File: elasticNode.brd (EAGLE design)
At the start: 58.2 x 52.5 mm, 130 parts, among them J1 FEMALE_HEADER_2X1, J2 JUMPER, J3 ISP_CONN_6PIN, J5 FEMALE_HEADER_10X2, J6 USB_CONNMICRO_SMT, M1 SISS23DN, M2 SISS23DN, M3 SISS23DN, U1 AT90USB128, U10 LTC3419DFN, U11 PAC1720, U14 LTC3419DFN, U2 IS66WV51216EALL, U3 MRF24J40MA, U4 SPARTAN7-LX15, U6 SST26VF032BWDFN, U7 PAC1720, U8 PAC1720, U9 PAC1720, X1 8MHz, X2 50MHz, X3 32MHz, X4 100MHz

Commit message: back up before review.
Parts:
- removed C26: 22u, passive:0805
- removed J3: ISP_CONN_6PIN, connectors:ICSP_SMT
- removed L5: 3.3uH, passive:0805
- removed R29, R30, R44, R45, R48, R49: 1.5k, passive:0805
- removed R37, R38: 1k5, passive:0805
- removed TP4, TP5, TP6: TEST_POINTTHT, connectors:THT
- added C6, C9: 20p, passive:0805
- added D11, D12: GREEN 2.2V, opto:0805
- added J7: USB_CONNMICRO_SMT, connectors:USB_MICRO_B_SMT
- added M4: SISS23DN, power:POWERPAK1212-8
- added MCU_PROGRAM, MON_PROGRAM: ISP_CONN_6PIN, connectors:ICSP_SMT
- added R50, R51: 550, passive:0805
- added R52, R53: 22, passive:0805
- added R54: 15k, passive:0805
- added TP7, TP8: TEST_POINTTHT, connectors:THT
- added U5: ATMEGA32U4QFN, ic:QFN44
- added X5: 8MHz, passive:3.2X2.5_OSC
- moved C30 195.2 mm to (42.4, 27.8)
- moved C34 195.2 mm to (43.1, 24.3)
- moved C38 195.2 mm to (42.4, 18.8)
- moved C39 195.2 mm to (45.2, 18.8)
- moved C32 195.2 mm to (42.4, 13.6)
- moved C35 195.2 mm to (46.6, 25.2)
- moved C36 195.2 mm to (42.4, 21.4)
- moved C37 195.2 mm to (45.2, 21.4)
- moved C40 195.2 mm to (42.4, 16.2)
- moved U2 173.2 mm to (8.30, 29.8)
- moved C20 148.3 mm to (36.2, 36.8)
- moved C24 148.3 mm to (36.9, 25.4)
- moved C25 148.3 mm to (40.4, 26.3)
- moved C29 148.3 mm to (36.2, 22.5)
- moved C31 148.3 mm to (36.2, 19.9)
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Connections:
- net A10 renamed XMEM_A10
- net A11 renamed XMEM_A11
- net A12 renamed XMEM_A12
- net A13 renamed XMEM_A13
- net A14 renamed XMEM_A14
- net A15 renamed XMEM_A15
- net A8 renamed XMEM_A8
- net A9 renamed XMEM_A9
- net RD renamed XMEM_RD
- net WR renamed XMEM_WR
- removed net 1V2: C26.2, L5.2, R37.2, TP3.3
- removed net 1V5: TP6.3
- removed net ENABLE_LEDS: U1.17
- removed net FPGA_RESES: U1.59
- removed net FPGA_SUSPEND: U1.19
- removed net N$21: U4.P4
- removed net N$22: U4.P3
- removed net N$26: U4.L3
- removed net N$31: U4.L2
- removed net N$33: U4.M5
- removed net N$34: U4.M4
- removed net N$35: U4.P5
- removed net N$36: U4.N4
- removed net N$39: U4.H12
- removed net N$40: U4.L5
- removed net N$54: R37.1, R38.2, U14.8
- removed net N$56: L5.1, U14.6
- removed net SRAM_VCC: R23.2, R43.2, U11.2, U4.G2, U4.K2, U4.N2, U7.2, X4.1, X4.4
- new net DAUGHTER_VCC: OUT2.10, R43.2, U11.2
- new net GND1: D11.2, D12.2
- new net MON_LED0: R50.1, U5.20
- new net MON_LED1: R51.1, U5.21
- new net MON_MISO: MON_PROGRAM.1, U5.11
- new net MON_MOSI: MON_PROGRAM.4, U5.10
- new net MON_RESET: MON_PROGRAM.5, R54.2, U5.13
- new net MON_SCK: MON_PROGRAM.3, U5.9
- new net MON_USB_D+: R53.1, U5.4
- new net MON_USB_D-: R52.1, U5.3
- new net MON_USB_VCC: J7.1, U5.7
- new net N$16: D12.1, R51.2
- new net N$17: D11.1, R50.2
- new net N$18: C9.1, U5.17, X5.3
- new net N$19: J7.2, R52.2
- new net N$20: C6.1, U5.16, X5.1
- new net SRAM_POWER: M4.4, U1.2
- new net SRAM_VDD_MON: M4.1, M4.2, M4.3, R23.2, U7.2
- net 1V: now also TP8.3; no longer TP4.3
- net 1V8: now also TP7.3; no longer R43.1, TP2.3, U11.1
- net 3V3: now also MCU_PROGRAM.2, MON_PROGRAM.2, R43.1, R54.1, TP2.3, U11.1, U5.14, U5.2, U5.24, U5.34, U5.44, U5.6; no longer J3.2, OUT2.10, R29.2, R30.2, R44.2, R45.2, R48.2, R49.2, U14.7
- net AD6/SELECTMAP_D1/SPI_MISO/MCU_PDO: now also MCU_PROGRAM.1; no longer J3.1
- net AD7/SELECTMAP_D0/SPI_MOSI/PDI: now also MCU_PROGRAM.4; no longer J3.4
- net FPGA_RESET: now also U1.59
- net GND: now also C2.2, C3.2, C6.2, C9.2, J7.5, MCU_PROGRAM.6, MON_PROGRAM.6, TP3.3, U5.15, U5.23, U5.35, U5.43, U5.45, U5.5; no longer C26.1, J3.6, R38.1, TP5.3
- net MCU_RESET: now also MCU_PROGRAM.5; no longer J3.5
- net MONITORING: now also U5.1
- net N$5: now also J7.3, R53.2; no longer C2.2, C3.2
- net SCL: now also U5.18; no longer R29.1, R44.1, R48.1
- net SDA: now also U5.19; no longer R30.1, R45.1, R49.1
- net SPI_SCK/CCLK: now also MCU_PROGRAM.3; no longer J3.3
- net SRAM_VDD: now also M4.5, M4.6, M4.7, M4.8, U4.G2, U4.K2, U4.N2, X4.1, X4.4

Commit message: Layout work start.
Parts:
- removed C18: 10u, passive:0805
- removed D10: RED, opto:0805
- removed R39: 6k8, passive:0805
- removed R40: 270, passive:0805
- removed R46: 10k, passive:0805
- added C12, C15: 10u, passive:0805
- added J3: JUMPER, connectors:JUMPER_SMT
- added R29, R30: 15k, passive:0805
- added R37: 1k5, passive:0805
- added R38: 6k8, passive:0805
- R31: value 6k8 -> 10k
- R32: value 1k5 -> 6k8
- moved R1 157.5 mm to (204.6, 66.6)
- moved R2 157.5 mm to (204.6, 64.9)
- moved U7 117.0 mm to (93.3, 80.1), flipped to the top, turned to 0 degrees
- moved R26 111.2 mm to (93.4, 77.0), flipped to the top, turned to 0 degrees
- moved D9 107.1 mm to (-20.8, -56.9), turned to 0 degrees
- moved R20 107.0 mm to (89.9, 78.9), flipped to the top
- moved R23 105.8 mm to (89.9, 81.9), flipped to the top
- moved R33 101.6 mm to (-20.8, -54.8), turned to 0 degrees
- moved U11 98.5 mm to (93.3, 60.4)
- moved R43 98.3 mm to (89.9, 62.2), turned to 90 degrees
- moved U8 97.6 mm to (93.3, 73.4), flipped to the top
- moved R27 97.6 mm to (93.4, 70.3), flipped to the top
- moved R36 97.4 mm to (89.9, 59.2), turned to 90 degrees
- moved R42 97.2 mm to (19.5, 99.4)
- moved R41 95.2 mm to (16.7, 99.4)
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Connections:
- removed net N$1: L1.2, U10.4
- removed net N$57: D10.2, R40.2
- removed net N$8: L2.1, U10.6
- new net MON_HWB: J3.1, R30.2, U5.33
- new net N$21: R29.1, U5.2
- new net N$22: L1.1, U10.4
- new net N$26: L2.2, U10.6
- net 1V: now also C17.1, L1.2, R31.2; no longer C27.1, L6.1, R46.2
- net 1V8: now also L2.1, R23.2, R47.1; no longer L2.2, R23.1, R47.2
- net 3V3: now also C12.1, C27.1, L6.1, R24.2, R29.2, R30.1, R38.2, R43.2; no longer C17.1, L1.1, R24.1, R31.1, R43.1, U5.2
- net 5V: now also C15.1; no longer C18.1, D10.1, D9.1
- net DAUGHTER_VCC: now also R43.1; no longer R43.2
- net GND: now also C12.2, C15.2, J3.2, R37.2; no longer C18.2, R39.2, R40.1
- net MONITORING: now also U1.1
- net N$2: now also R31.1; no longer R31.2
- net N$53: now also R37.1, R38.1; no longer R39.1, R46.1
- net N$7: now also R47.2; no longer R47.1
- net SRAM_VDD_MON: now also R23.1; no longer R23.2
- net USB_VCC_RAW: now also D9.1
- net WIRELESS_VCC: now also R24.1; no longer R24.2

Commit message: backup
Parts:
- R29: value 15k -> 0
- moved R1 163.6 mm to (47.4, 21.0)
- moved R2 163.6 mm to (47.4, 19.3)
- moved R54 119.1 mm to (50.6, 41.8), turned to 0 degrees
- moved D9 100.9 mm to (47.4, 17.4), turned to 180 degrees
- moved R29 100.2 mm to (50.6, 40.3)
- moved R33 98.1 mm to (47.4, 15.7), turned to 180 degrees
- moved R26 90.5 mm to (7.20, 49.4), flipped to the bottom, turned to 180 degrees
- moved U7 87.6 mm to (10.9, 50.3), flipped to the bottom
- moved C12 87.1 mm to (28.4, 39.9), turned to 90 degrees
- moved R23 81.2 mm to (14.7, 51.2), flipped to the bottom, turned to 0 degrees
- moved R20 80.8 mm to (14.7, 49.4), flipped to the bottom, turned to 0 degrees
- moved R28 77.1 mm to (17.6, 49.5), flipped to the bottom, turned to 180 degrees
- moved C32 76.4 mm to (12.1, 31.6), flipped to the bottom
- moved R30 75.8 mm to (36.9, 36.7), turned to 0 degrees
- moved U9 73.8 mm to (21.4, 50.3), flipped to the bottom
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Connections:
- net DAUGHTER_VCC: now also R24.1, U8.2; no longer R43.1, U11.2
- net WIRELESS_VCC: now also R43.1, U11.2; no longer R24.1, U8.2
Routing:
- removed copper zone on layer 16, net 1V
- removed copper zone on layer 16, net 3V3
- removed copper zone on layer 16, net 5V
- removed copper zone on layer 16, net N$1
- removed copper zone on layer 16, net N$8
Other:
- board text added: "FPGA LEDS"
- board text added: "MON LEDS"
- board text removed: "FPGA"
- board text removed: "LEDS"

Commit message: backup
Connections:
- net SRAM_A0: no longer U4.D3
- net SRAM_A1: no longer U4.C3
- net SRAM_A10: now also U4.M5; no longer U4.C5
- net SRAM_A11: now also U4.N1; no longer U4.C4
- net SRAM_A12: no longer U4.E4
- net SRAM_A13: no longer U4.D4
- net SRAM_A14: no longer U4.F3
- net SRAM_A15: no longer U4.F2
- net SRAM_A16: no longer U4.G1
- net SRAM_A17: now also U4.N4; no longer U4.F1
- net SRAM_A18: now also U4.M2; no longer U4.E2
- net SRAM_A2: no longer U4.A4
- net SRAM_A3: no longer U4.A3
- net SRAM_A4: now also U4.A5; no longer U4.B3
- net SRAM_A5: now also U4.A4; no longer U4.A2
- net SRAM_A6: now also U4.A3; no longer U4.B5
- net SRAM_A7: now also U4.A2; no longer U4.A5
- net SRAM_A8: now also U4.M3; no longer U4.B2
- net SRAM_A9: now also U4.M4; no longer U4.B1
- net SRAM_CS: no longer U4.B6
- net SRAM_D0: no longer U4.D2
- net SRAM_D1: no longer U4.D1
- net SRAM_D10: now also U4.L1; no longer U4.K3
- net SRAM_D11: now also U4.L2; no longer U4.J4
- net SRAM_D12: now also U4.J1; no longer U4.J3
- net SRAM_D13: now also U4.H1; no longer U4.M1
- net SRAM_D14: now also U4.G1; no longer U4.L1
- net SRAM_D15: now also U4.F1; no longer U4.M3
- net SRAM_D2: no longer U4.C1
- net SRAM_D3: no longer U4.H4
- net SRAM_D4: no longer U4.H3
- net SRAM_D5: no longer U4.H2
- net SRAM_D6: no longer U4.H1
- net SRAM_D7: no longer U4.J2
- net SRAM_D8: now also U4.M1; no longer U4.J1
- net SRAM_D9: now also U4.L3; no longer U4.K4
- net SRAM_LB: now also U4.D1; no longer U4.N1
- net SRAM_OE: now also U4.B1; no longer U4.M2
- net SRAM_UB: now also U4.C1; no longer U4.P2
- net SRAM_WE: no longer U4.F4
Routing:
- net SRAM_VDD: track 0.00 -> 56.4 mm, vias 0 -> 6
- net SRAM_A4: track 0.00 -> 19.8 mm, vias 0 -> 2
- net SRAM_A10: track 0.00 -> 8.77 mm, vias 0 -> 2
- net SRAM_A17: track 0.00 -> 8.73 mm, vias 0 -> 2
- net SRAM_A5: track 0.00 -> 7.04 mm
- net SRAM_A9: track 0.00 -> 6.95 mm, vias 0 -> 2
- net SRAM_D9: track 0.00 -> 6.24 mm, vias 0 -> 2
- net SRAM_A6: track 0.00 -> 6.04 mm
- net SRAM_A8: track 0.00 -> 5.62 mm, vias 0 -> 2
- net SRAM_A7: track 0.00 -> 5.08 mm
- net SRAM_D12: track 0.00 -> 5.06 mm
- net SRAM_A11: track 0.00 -> 4.79 mm
- net SRAM_D11: track 0.00 -> 4.77 mm, vias 0 -> 2
- net SRAM_A18: track 0.00 -> 4.46 mm, vias 0 -> 2
- net SRAM_D10: track 0.00 -> 4.04 mm
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
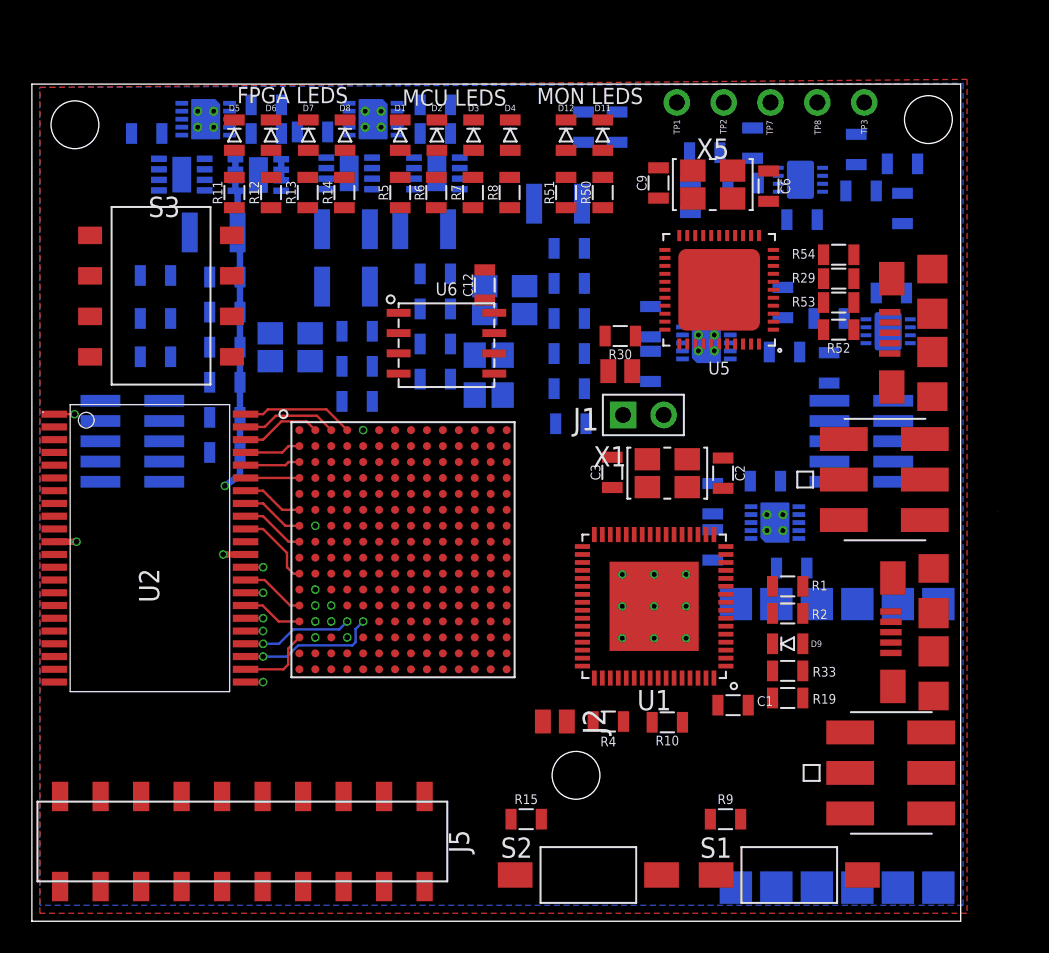
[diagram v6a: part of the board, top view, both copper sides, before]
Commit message: backup
SRAM and FPGA finished, now connecting fpga and MCU
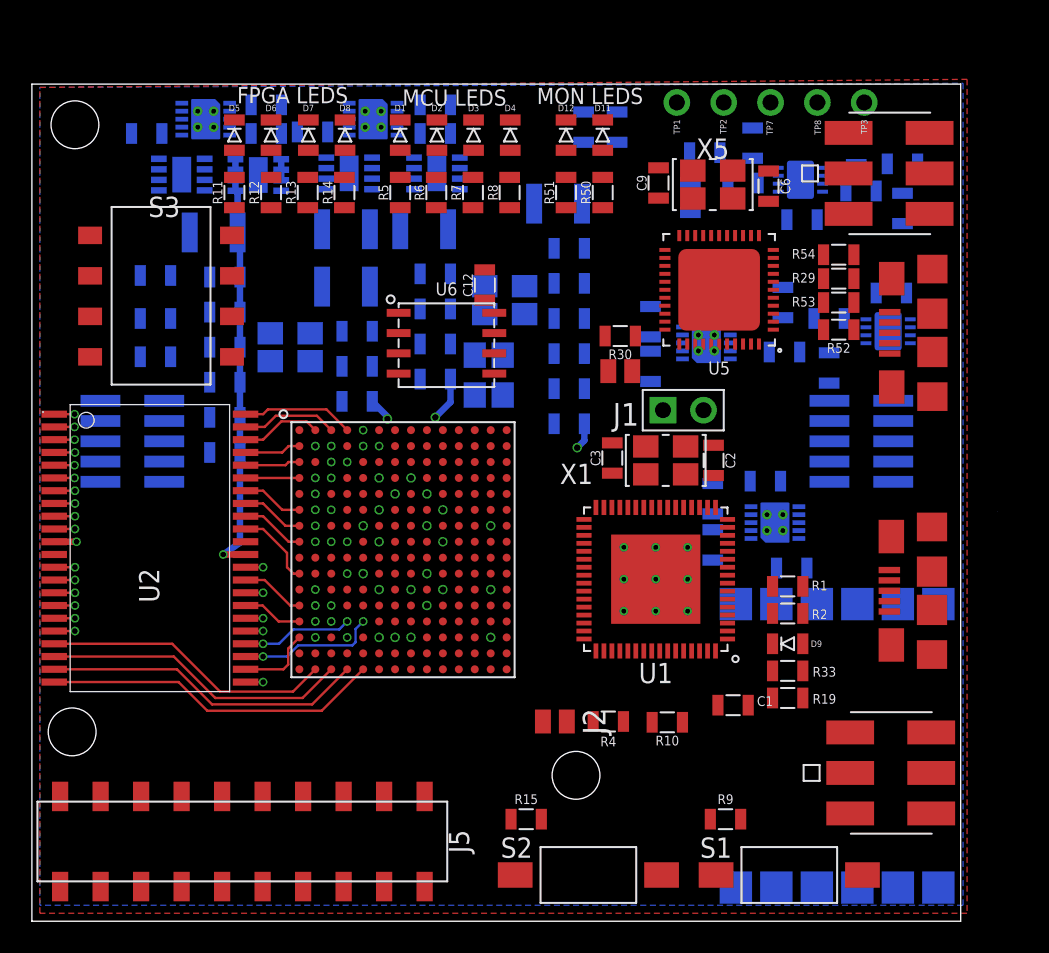
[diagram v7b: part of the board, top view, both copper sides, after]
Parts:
- moved MON_PROGRAM 19.2 mm to (53.8, 46.9)
- moved J6 2.60 mm to (53.8, 20.7)
- moved J1 2.52 mm to (40.9, 32.0)
- moved U1 1.70 mm to (39.1, 21.4)
- moved C2 1.00 mm to (42.8, 28.9)
- moved C3 0.90 mm to (36.4, 29.1)
- moved X1 0.81 mm to (39.8, 28.9)
- moved C40 0.10 mm to (33.7, 31.2)
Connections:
- new net N$52: U4.L14
- net AD0/SELECTMAP_D7: no longer U4.B14
- net AD1/SELECTMAP_D6: no longer U4.B13
- net AD2/SELECTMAP_D5/MCU_RX1: no longer U4.A13
- net AD3/SELECTMAP_D4/MCU_TX1: no longer U4.A12
- net AD4/SELECTMAP_D3/FPGA_HOLD: no longer U4.C10
- net AD5/SELECTMAP_D2/FPGA_WP: no longer U4.D10
- net AD6/SELECTMAP_D1/SPI_MISO/MCU_PDO: no longer U4.B12
- net AD7/SELECTMAP_D0/SPI_MOSI/PDI: no longer U4.B11
- net ALE/HWB: no longer U4.G11
- net FPGA_LED0: no longer U4.E11
- net FPGA_LED1: no longer U4.B10
- net FPGA_LED2: no longer U4.A10
- net FPGA_LED3: no longer U4.C12
- net SPI_CS: no longer U4.C11, U4.L14
- net SRAM_A0: now also U4.B2
- net SRAM_A1: now also U4.B3
- net SRAM_A12: now also U4.P5
- net SRAM_A13: now also U4.P4
- net SRAM_A14: now also U4.P3
- net SRAM_A15: now also U4.P2
- net SRAM_A16: now also U4.J4
- net SRAM_A2: now also U4.B5
- net SRAM_A3: now also U4.B6
- net SRAM_CS: now also U4.C4
- net SRAM_D0: now also U4.C3
- net SRAM_D1: now also U4.D2
- net SRAM_D2: now also U4.D3
- net SRAM_D3: now also U4.E2
- net SRAM_D4: now also U4.F2
- net SRAM_D5: now also U4.F3
- net SRAM_D6: now also U4.H4
- net SRAM_D7: now also U4.H2
- net SRAM_WE: now also U4.H3
- net XMEM_A10: now also U4.B13; no longer U4.E13
- net XMEM_A11: no longer U4.D13
- net XMEM_A12: now also U4.C12, U4.C14; no longer U4.G14
- net XMEM_A13: now also U4.D12; no longer U4.F14
- net XMEM_A14: no longer U4.F13
- net XMEM_A15: no longer U4.F12
- net XMEM_A8: now also U4.B12; no longer U4.E12
- net XMEM_A9: now also U4.B14; no longer U4.D12
- net XMEM_RD: now also U4.A13; no longer U4.C14
- net XMEM_WR: now also U4.A12; no longer U4.D14
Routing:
- net FPGA_VCCIO: track 0.00 -> 39.1 mm, vias 0 -> 6
- net FPGA_VCCINT: track 0.00 -> 28.9 mm, vias 0 -> 13
- net SRAM_A12: track 0.00 -> 21.2 mm
- net SRAM_A3: track 0.00 -> 20.9 mm, vias 0 -> 2
- net SRAM_A16: track 0.00 -> 20.7 mm, vias 0 -> 2
- net SRAM_A13: track 0.00 -> 20.2 mm
- net SRAM_D6: track 0.00 -> 20.1 mm, vias 0 -> 2
- net FPGA_VCCAUX: track 0.00 -> 20.1 mm, vias 0 -> 6
- net SRAM_A2: track 0.00 -> 19.9 mm, vias 0 -> 2
- net SRAM_WE: track 0.00 -> 19.5 mm, vias 0 -> 2
- net SRAM_CS: track 0.00 -> 19.2 mm, vias 0 -> 2
- net SRAM_D5: track 0.00 -> 19.2 mm, vias 0 -> 2
- net SRAM_A14: track 0.00 -> 19.2 mm
- net SRAM_D2: track 0.00 -> 18.4 mm, vias 0 -> 2
- net SRAM_A15: track 0.00 -> 18.3 mm
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
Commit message: back up
spi_sck didn’t connect to FPGA,OK？
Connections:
- net AD6/SELECTMAP_D1/SPI_MISO/MCU_PDO: now also U4.B12
- net AD7/SELECTMAP_D0/SPI_MOSI/PDI: now also U4.B11
- net FPGA_LED0: now also U4.D10
- net FPGA_LED1: now also U4.C10
- net FPGA_LED2: now also U4.B10
- net FPGA_LED3: now also U4.A10
- net XMEM_A10: no longer U4.B13
- net XMEM_A12: no longer U4.C12, U4.C14
- net XMEM_A13: no longer U4.D12
- net XMEM_A8: no longer U4.B12
- net XMEM_A9: no longer U4.B14
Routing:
- net MCU_LED0: track 0.00 -> 29.1 mm
- net FPGA_LED0: track 0.00 -> 27.4 mm, vias 0 -> 2
- net MCU_LED1: track 0.00 -> 27.3 mm
- net MCU_LED2: track 0.00 -> 25.7 mm
- net FPGA_LED1: track 0.00 -> 23.9 mm, vias 0 -> 2
- net MCU_LED3: track 0.00 -> 23.8 mm
- net FPGA_LED2: track 0.00 -> 20.9 mm, vias 0 -> 2
- net FPGA_LED3: track 0.00 -> 18.3 mm
- net OSC_32: track 0.00 -> 17.7 mm, vias 0 -> 1
- net XMEM_WR: track 0.00 -> 12.9 mm
- net XMEM_RD: track 0.00 -> 12.4 mm
- net MON_LED1: track 0.00 -> 8.68 mm
- net OSC_50: track 0.00 -> 7.61 mm, vias 0 -> 1
- net MON_LED0: track 0.00 -> 6.82 mm
